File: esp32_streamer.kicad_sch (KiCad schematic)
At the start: 39 parts, among them J2 SJ1-3533NS, U1 PCM5122PW, U2 ESP32-WROVER-EM213EH2864PH3Q0

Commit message: Updates to schematic - nearly complete
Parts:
- added D1, D2: LED_R, symbol Device:LED
- added J3: Conn_01x04_Male, Connector_PinHeader_2.54mm:PinHeader_1x04_P2.54mm_Horizontal, symbol Connector:Conn_01x04_Male
- added R? (x2): 2k, Resistor_SMD:R_0603_1608Metric, symbol Device:R
- gave numbers to parts that had none: 5
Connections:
- net +3V3: now also R?.1
- net GND: now also D1.1 (K), D2.1 (K), J3.4 (Pin_4)
- net VBUS: now also J3.1 (Pin_1)
- net GPIO12: now reaches U2.14 (IO12)
- net GPIO12: now also R?.1
- net ESP32_Rx: now reaches U2.34 (RXD0)
- net ESP32_Rx: now also J3.3 (Pin_3)
- net ESP32_Tx: now reaches U2.35 (TXD0)
- net ESP32_Tx: now also J3.2 (Pin_2)
- new net: D2.2 (A), R?.2
- new net: D1.2 (A), R?.2
- no-connect marks 21 -> 38
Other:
- note added: "Analogue Power Filtering"
- note added: "ESP32"
- note added: "ESP32 Pin Header (for flashing)"
- note added: "Notes - First iteration of ESP32-based DAC - No ESD protection on header pins - No ESD protection on analogue line out - PCM5122 DAC connected in 'hardwired' mode (no I2C controls) - One shared Digital / Analog GDN pane"
- note added: "PCM5122 DAC & Analogue Stage Line Out"
- note added: "USB Power, Filtering & LDOs"
- note removed: "TODO Ferrite beads (for analogue VCC and AGND) - DONE Rx Tx header for programming(and power) Power LED Bigger LDO? The one on this is tiny. - DONE Maybe Rx Tx leds USB-C for power - DONE ESD - use Varistor - DONE USB - do not connect shield to ground - DONE Shield for audio jack - do I leave unconnected or GDNed? Filtering for Analogue VA? 10R and 47u x 4 RC filter (low cutoff freq) ESD/ Varisto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"
- company: (none) -> Pavlos Papaefstathiou
- title: DAC and ESP32 streamer -> ESP32 Network DAC
- moved on the sheet: C1, C10, C11, C12, C13, C14, C15, C16, C17, C18, C19, C2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

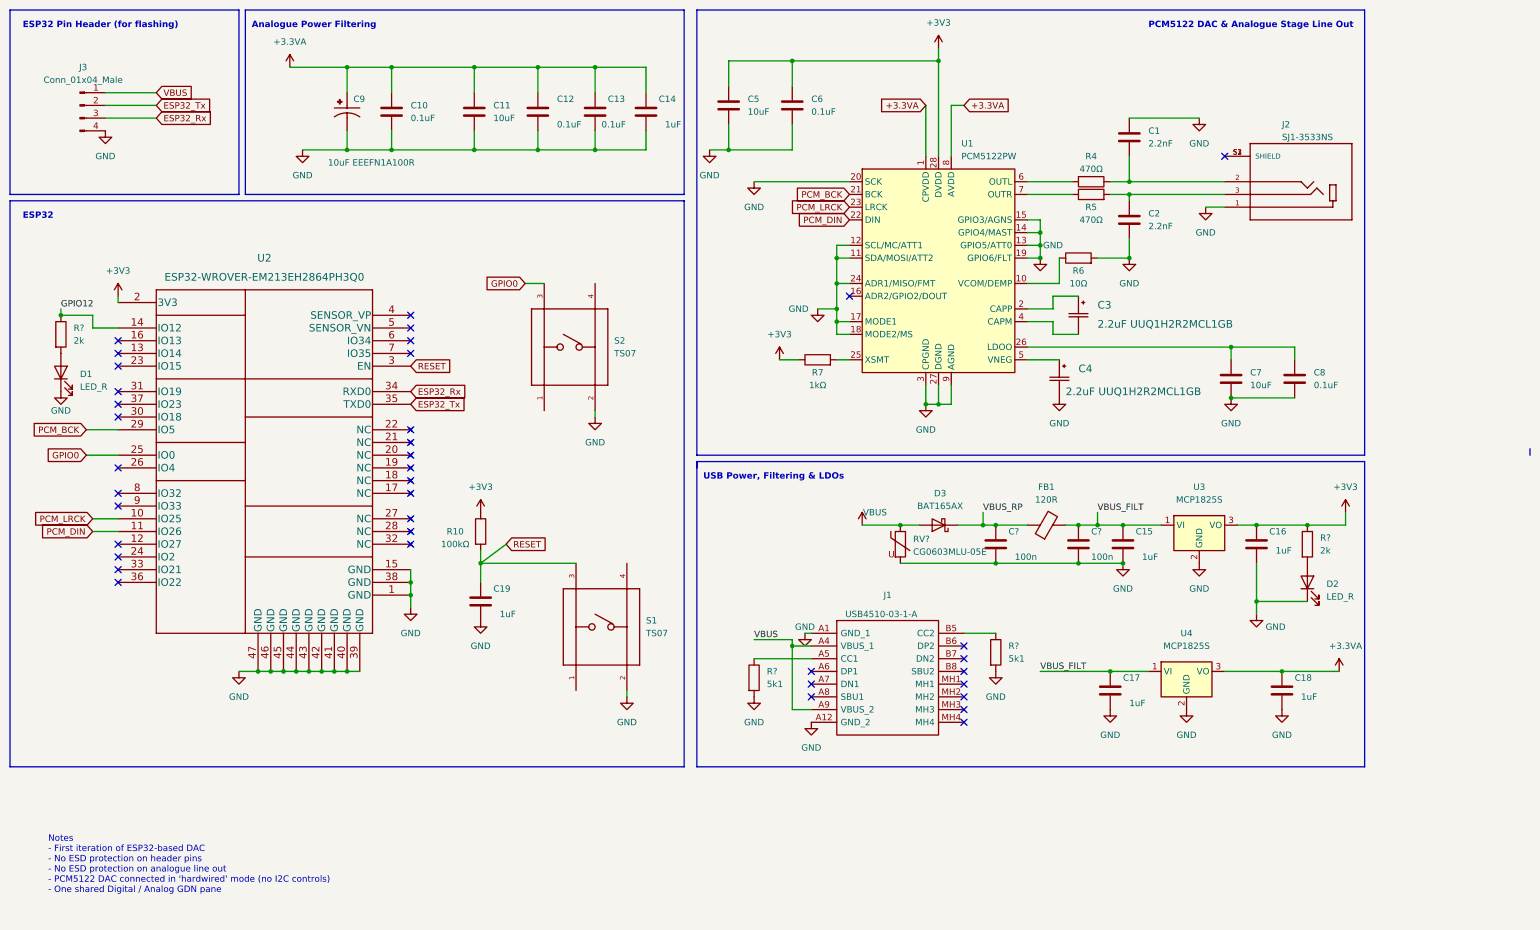
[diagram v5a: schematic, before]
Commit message: Updates and fixes based on ERC checks
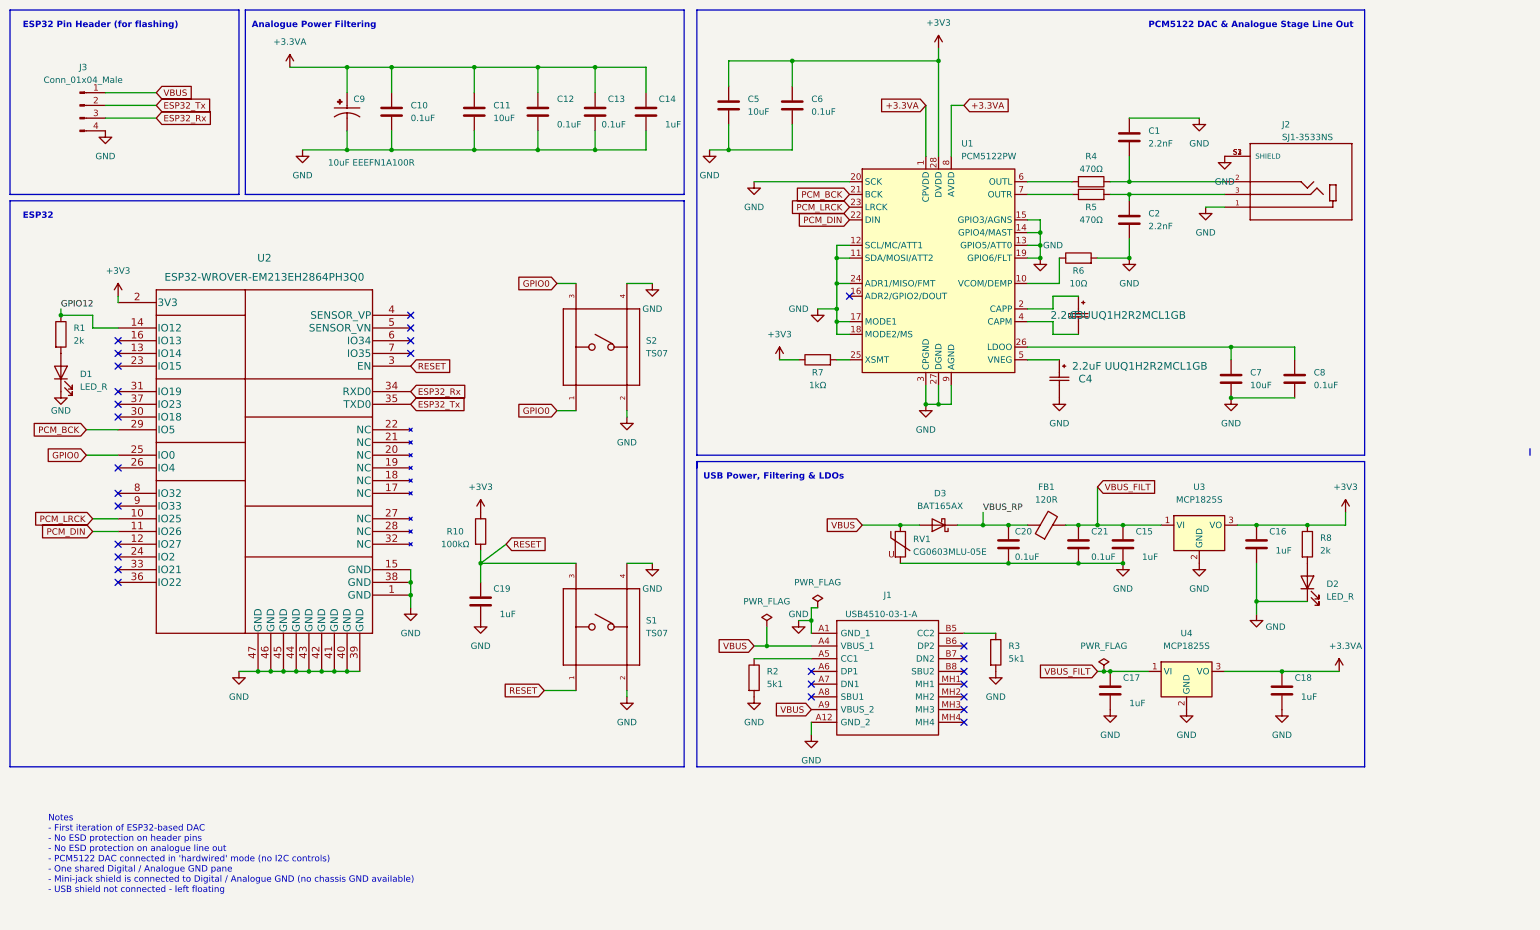
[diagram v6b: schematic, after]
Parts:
- C20, C21: renamed from C?; value 100n -> 0.1uF
- C3, C4: footprint CAP_UUQ_4X5P4_NCH -> library:UUQ1H2R2MCL1GB
- C9: footprint CAP_EEEFN1A100R -> library:CAP_EEEFN1A100R
- D1, D2: footprint (none) -> LED_SMD:LED_0603_1608Metric
- J2: AVAILABILITY Unavailable -> (none); PACKAGE None -> (none); PRICE None -> (none)
- R2, R3: renamed from R?; footprint (none) -> Resistor_SMD:R_0603_1608Metric
- gave numbers to parts that had none: 3
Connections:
- net GND: now also J2.S1 (SHIELD), J2.S2 (SHIELD), J2.S3 (SHIELD), S1.4, S2.4
- net GPIO0: now also S2.1
- net RESET: now also S1.1
- no-connect marks 38 -> 28
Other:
- note added: "Notes - First iteration of ESP32-based DAC - No ESD protection on header pins - No ESD protection on analogue line out - PCM5122 DAC connected in 'hardwired' mode (no I2C controls) - One shared Digital / Analogue GND pane - Mini-jack shield is connected to Digital / Analogue GND (no chassis GND available) - USB shield not connected - left floating"
- note removed: "Notes - First iteration of ESP32-based DAC - No ESD protection on header pins - No ESD protection on analogue line out - PCM5122 DAC connected in 'hardwired' mode (no I2C controls) - One shared Digital / Analog GDN pane"
- moved on the sheet: C20, S2

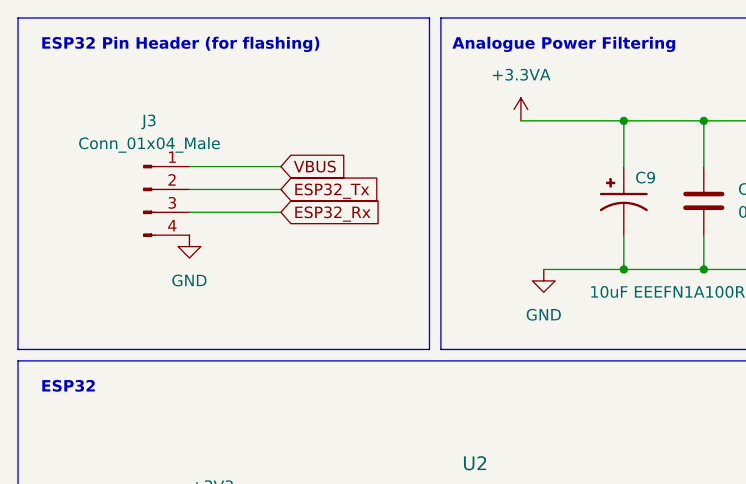
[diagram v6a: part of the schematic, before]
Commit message: Added more traces and a ground plane
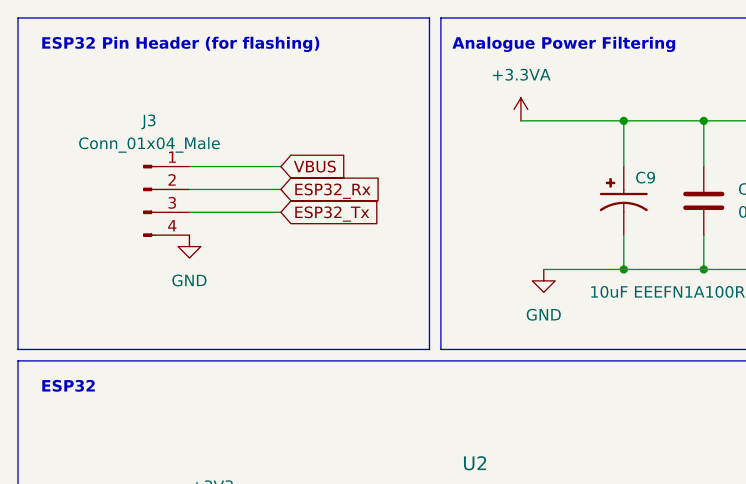
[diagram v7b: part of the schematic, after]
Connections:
- net ESP32_Rx: now also J3.2 (Pin_2); no longer J3.3 (Pin_3)
- net ESP32_Tx: now also J3.3 (Pin_3); no longer J3.2 (Pin_2)

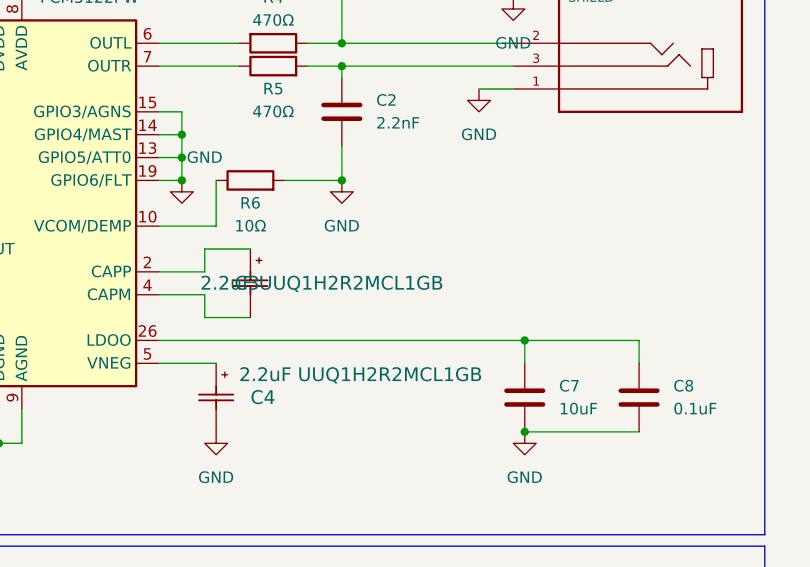
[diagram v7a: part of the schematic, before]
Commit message: Fixes to footprints and added more traces. Need to fix all DRC errors & warnings next.
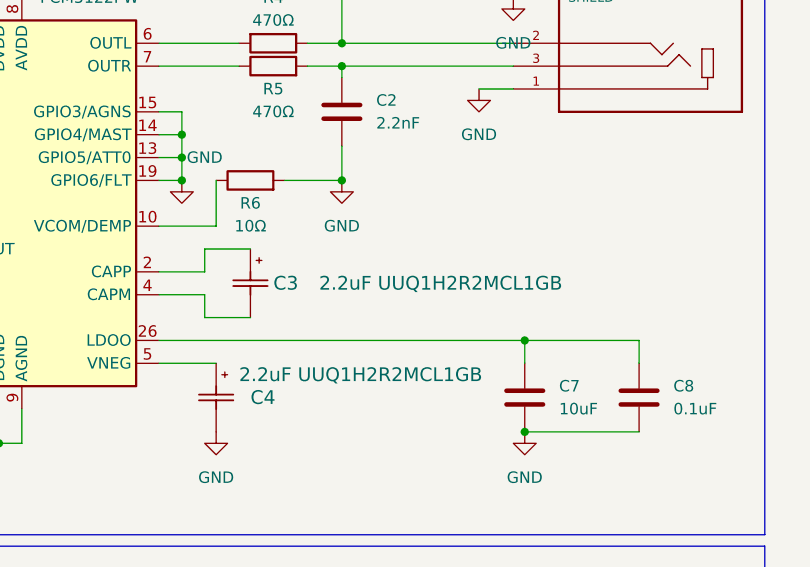
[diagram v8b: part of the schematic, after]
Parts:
- C11, C5: footprint Capacitor_SMD:C_0805_2012Metric -> Capacitor_SMD:C_1206_3216Metric
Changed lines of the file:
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@@
       (effects (font (size 1.27 1.27)) (justify left))
     )
-    (property "Footprint" "Capacitor_SMD:C_0805_2012Metric" (id 2) (at 158.4452 35.56 0)
+    (property "Footprint" "Capacitor_SMD:C_1206_3216Metric" (id 2) (at 158.4452 35.56 0)
       (effects (font (size 1.27 1.27)) hide)
     )
@@
       (effects (font (size 1.27 1.27)) (justify left))
     )
-    (property "Footprint" "Capacitor_SMD:C_0805_2012Metric" (id 2) (at 107.6452 36.83 0)
+    (property "Footprint" "Capacitor_SMD:C_1206_3216Metric" (id 2) (at 107.6452 36.83 0)
       (effects (font (size 1.27 1.27)) hide)
     )
@@
   )
   (symbol (lib_id "Nichicon UUQ1H2R2MCL1GB:UUQ1H2R2MCL1GB") (at 227.33 69.85 270) (unit 1)
-    (in_bom yes) (on_board yes) (fields_autoplaced)
-    (property "Reference" "C3" (id 0) (at 225.5584 73.66 90)
+    (in_bom yes) (on_board yes)
+    (property "Reference" "C3" (id 0) (at 229.87 73.66 90)
       (effects (font (size 1.524 1.524)) (justify left))
     )
-    (property "Value" "2.2uF UUQ1H2R2MCL1GB" (id 1) (at 221.7484 73.66 90)
+    (property "Value" "2.2uF UUQ1H2R2MCL1GB" (id 1) (at 234.95 73.66 90)
       (effects (font (size 1.524 1.524)) (justify left))
     )
@@
     )
     (path "/0939bf1c-3b01-4a1d-a6fe-f5720dfc5d1d"
-      (reference "C5") (unit 1) (value "10uF") (footprint "Capacitor_SMD:C_0805_2012Metric")
+      (reference "C5") (unit 1) (value "10uF") (footprint "Capacitor_SMD:C_1206_3216Metric")
     )
     (path "/2579e624-9923-437c-843d-c0950777b59d"
@@
     )
     (path "/56d5cdc5-bc51-4535-98bf-663eff88b79b"
-      (reference "C11") (unit 1) (value "10uF") (footprint "Capacitor_SMD:C_0805_2012Metric")
+      (reference "C11") (unit 1) (value "10uF") (footprint "Capacitor_SMD:C_1206_3216Metric")
     )
     (path "/238b950a-d9b1-4955-86d1-cbfd6f69cac5"
